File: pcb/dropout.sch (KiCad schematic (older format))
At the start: 61 parts, among them SW1 Rotary_Encoder_Switch, SW2 SW_Push, U1 ProMicro

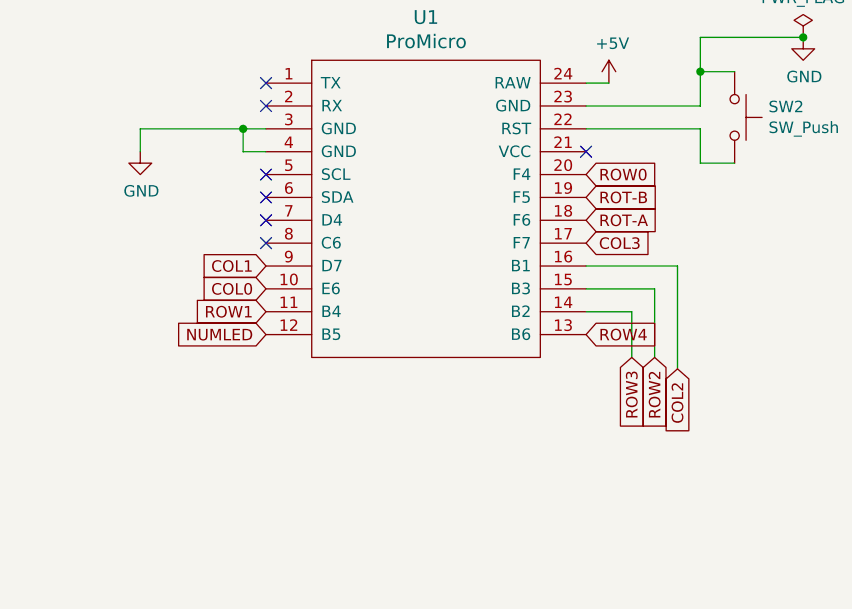
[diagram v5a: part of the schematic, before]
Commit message: flipping orientation of promicro for better clearance, now uses same pinout as rev0.1
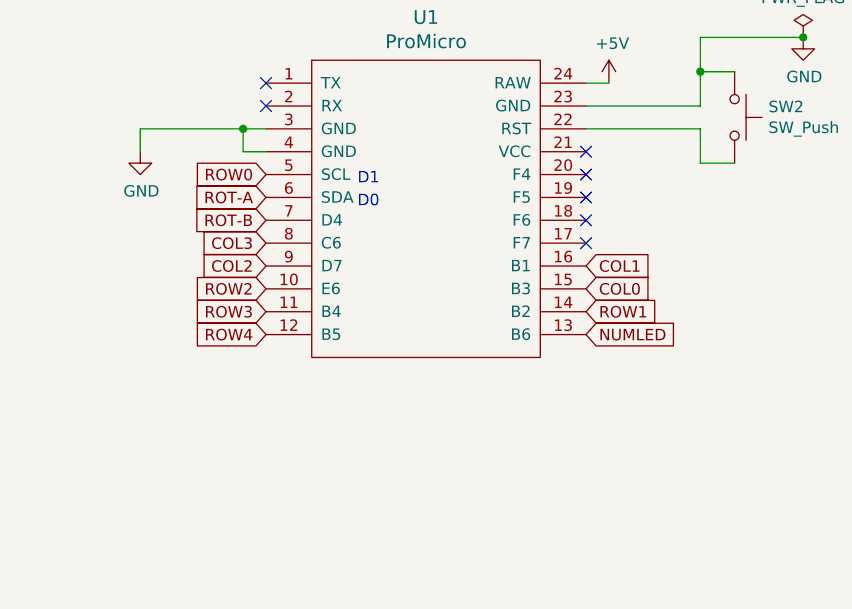
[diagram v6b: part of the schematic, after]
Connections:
- net COL0: now also U1.15 (B3); no longer U1.10 (E6)
- net COL1: now also U1.16 (B1); no longer U1.9 (D7)
- net COL2: now also U1.9 (D7); no longer U1.16 (B1)
- net COL3: now also U1.8 (C6); no longer U1.17 (F7)
- net NUMLED: now also U1.13 (B6); no longer U1.12 (B5)
- net ROT-A: now also U1.6 (SDA); no longer U1.18 (F6)
- net ROT-B: now also U1.7 (D4); no longer U1.19 (F5)
- net ROW0: now also U1.5 (SCL); no longer U1.20 (F4)
- net ROW1: now also U1.14 (B2); no longer U1.11 (B4)
- net ROW2: now also U1.10 (E6); no longer U1.15 (B3)
- net ROW3: now also U1.11 (B4); no longer U1.14 (B2)
- net ROW4: now also U1.12 (B5); no longer U1.13 (B6)
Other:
- note added: "D0"
- note added: "D1"
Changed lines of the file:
@@
 Wire Wire Line
 	4800 3350 4800 4200
-Text GLabel 5750 1850 2    50   Input ~ 0
-ROT-A
-Text GLabel 5750 1650 2    50   Input ~ 0
-ROT-B
 $Comp
 L power:GND #PWR03
@@
 	1    0    0    -1
 $EndComp
-$Comp
-L promicro:ProMicro U1
-U 1 1 5FCF7876
-P 7850 3750
-F 0 "U1" H 7850 4787 60  0000 C CNN
-F 1 "ProMicro" H 7850 4681 60  0000 C CNN
-F 2 "promicro:ProMico_mini&micro" H 7950 2700 60  0001 C CNN
-F 3 "" H 7950 2700 60  0000 C CNN
-	1    7850 3750
-	1    0    0    -1
-$EndComp
 Wire Wire Line
 	8550 3100 9050 3100
@@
 Wire Wire Line
 	6150 1750 6150 1950
-Text GLabel 8550 4100 2    50   Input ~ 0
+Text GLabel 7150 4100 0    50   Input ~ 0
 ROW4
-Text GLabel 8750 4200 3    50   Input ~ 0
+Text GLabel 7150 4000 0    50   Input ~ 0
 ROW3
-Text GLabel 8850 4200 3    50   Input ~ 0
+Text GLabel 7150 3900 0    50   Input ~ 0
 ROW2
-Text GLabel 7150 4000 0    50   Input ~ 0
+Text GLabel 8550 4000 2    50   Input ~ 0
 ROW1
-Text GLabel 8550 3400 2    50   Input ~ 0
+Text GLabel 7150 3400 0    50   Input ~ 0
 ROW0
-Text GLabel 7150 3900 0    50   Input ~ 0
+Text GLabel 8550 3900 2    50   Input ~ 0
 COL0
+Text GLabel 8550 3800 2    50   Input ~ 0
+COL1
 Text GLabel 7150 3800 0    50   Input ~ 0
-COL1
-Text GLabel 8950 4250 3    50   Input ~ 0
 COL2
 Text GLabel 4800 1050 1    50   Input ~ 0
 COL3
-Text GLabel 8550 3700 2    50   Input ~ 0
+Text GLabel 7150 3700 0    50   Input ~ 0
 COL3
-Text GLabel 7150 4100 0    50   Input ~ 0
+Text GLabel 8550 4100 2    50   Input ~ 0
 NUMLED
 $Comp
@@
 	1    0    0    -1
 $EndComp
-NoConn ~ 7150 3600
-NoConn ~ 7150 3700
 Wire Wire Line
 	4800 1050 4800 1400
-Wire Wire Line
-	8750 4200 8750 4000
-Wire Wire Line
-	8750 4000 8550 4000
-Wire Wire Line
-	8850 4200 8850 3900
-Wire Wire Line
-	8850 3900 8550 3900
-Wire Wire Line
-	8550 3800 8950 3800
-Wire Wire Line
-	8950 4250 8950 3800
 $Comp
 L Device:C C2
@@
 $EndComp
 Connection ~ 4800 1400
-Text GLabel 8550 3500 2    50   Input ~ 0
+Text GLabel 7150 3600 0    50   Input ~ 0
 ROT-B
-Text GLabel 8550 3600 2    50   Input ~ 0
+Text GLabel 7150 3500 0    50   Input ~ 0
 ROT-A
 Wire Wire Line
@@
 $EndComp
 Connection ~ 9500 2800
-NoConn ~ 7150 3400
-NoConn ~ 7150 3500
 NoConn ~ 8550 3300
+$Comp
+L promicro:ProMicro U1
+U 1 1 5FCF7876
+P 7850 3750
+F 0 "U1" H 7850 4787 60  0000 C CNN
+F 1 "ProMicro" H 7850 4681 60  0000 C CNN
+F 2 "promicro:ProMico_mini&micro" H 7950 2700 60  0001 C CNN
+F 3 "" H 7950 2700 60  0000 C CNN
+	1    7850 3750
+	1    0    0    -1
+$EndComp
+Text Notes 7550 3450 0    50   ~ 0
+D1
+Text Notes 7550 3550 0    50   ~ 0
+D0
+NoConn ~ 8550 3700
+NoConn ~ 8550 3600
+NoConn ~ 8550 3500
+NoConn ~ 8550 3400
+Text GLabel 5750 1850 2    50   Input ~ 0
+ROT-A
+Text GLabel 5750 1650 2    50   Input ~ 0
+ROT-B
 $EndSCHEMATC

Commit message: adding graphics to pcb, some cleanup
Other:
- note removed: "mini-usb\n"
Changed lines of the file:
@@
 Text Notes 9950 1200 0    50   ~ 0
 Holes for Base
-Text Notes 7700 2650 0    50   ~ 0
-mini-usb\n
 $Comp
 L MX_Alps_Hybrid:MX-NoLED K-FN1

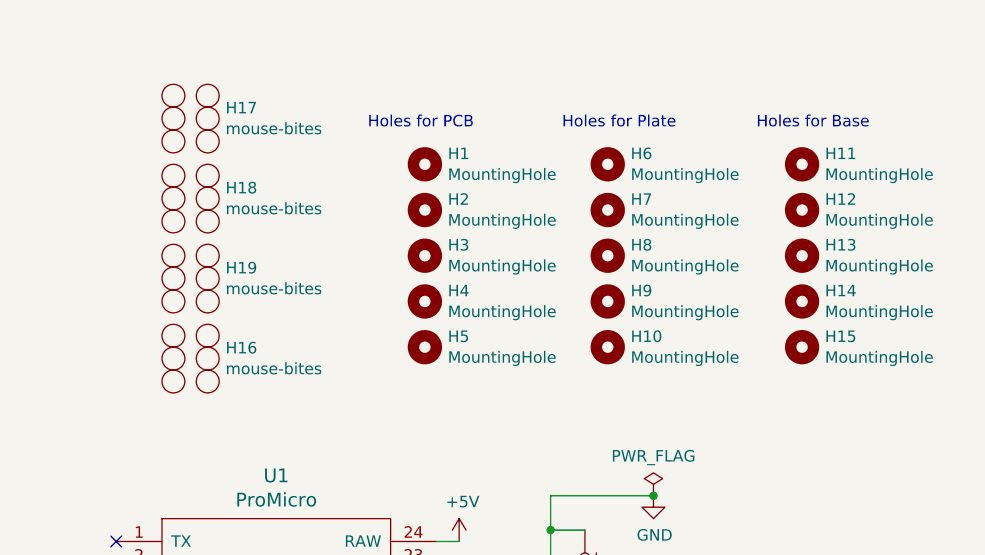
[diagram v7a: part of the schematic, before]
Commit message: breaking up panelization for production
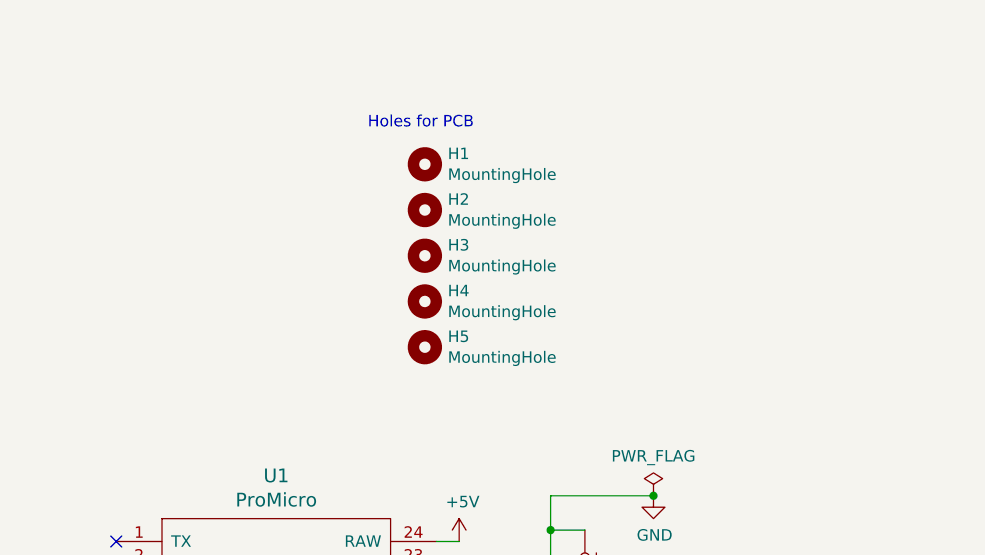
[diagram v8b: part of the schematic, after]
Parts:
- removed H10, H11, H12, H13, H14, H15, H6, H7, H8, H9: MountingHole, MountingHole:MountingHole_2.2mm_M2, symbol Mechanical:MountingHole
- removed H16, H17, H18, H19: mouse-bites, Keebio-Parts:breakaway-mousebites, symbol panelization:mouse-bites
- D1, D10, D11, D12, D13, D14, D15, D16, D17, D18, D2, D3, D4, D5, D6, D7, D8, D9: footprint footprint:Diode_TH_SOD123 -> Diodes_SMD:Diode_TH_SOD123
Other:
- note removed: "Holes for Base"
- note removed: "Holes for Plate"
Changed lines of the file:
@@
 F 0 "D6" H 2900 2067 50  0000 C CNN
 F 1 "D" H 2900 1976 50  0000 C CNN
-F 2 "footprint:Diode_TH_SOD123" H 2900 1850 50  0001 C CNN
+F 2 "Diodes_SMD:Diode_TH_SOD123" H 2900 1850 50  0001 C CNN
 F 3 "~" H 2900 1850 50  0001 C CNN
 	1    2900 1850
@@
 F 0 "D1" H 1950 2067 50  0000 C CNN
 F 1 "D" H 1950 1976 50  0000 C CNN
-F 2 "footprint:Diode_TH_SOD123" H 1950 1850 50  0001 C CNN
+F 2 "Diodes_SMD:Diode_TH_SOD123" H 1950 1850 50  0001 C CNN
 F 3 "~" H 1950 1850 50  0001 C CNN
 	1    1950 1850
@@
 F 0 "D10" H 3700 2067 50  0000 C CNN
 F 1 "D" H 3700 1976 50  0000 C CNN
-F 2 "footprint:Diode_TH_SOD123" H 3700 1850 50  0001 C CNN
+F 2 "Diodes_SMD:Diode_TH_SOD123" H 3700 1850 50  0001 C CNN
 F 3 "~" H 3700 1850 50  0001 C CNN
 	1    3700 1850
@@
 F 0 "D15" H 4450 2067 50  0000 C CNN
 F 1 "D" H 4450 1976 50  0000 C CNN
-F 2 "footprint:Diode_TH_SOD123" H 4450 1850 50  0001 C CNN
+F 2 "Diodes_SMD:Diode_TH_SOD123" H 4450 1850 50  0001 C CNN
 F 3 "~" H 4450 1850 50  0001 C CNN
 	1    4450 1850
@@
 F 0 "D2" H 1950 3067 50  0000 C CNN
 F 1 "D" H 1950 2976 50  0000 C CNN
-F 2 "footprint:Diode_TH_SOD123" H 1950 2850 50  0001 C CNN
+F 2 "Diodes_SMD:Diode_TH_SOD123" H 1950 2850 50  0001 C CNN
 F 3 "~" H 1950 2850 50  0001 C CNN
 	1    1950 2850
@@
 F 0 "D7" H 2900 3067 50  0000 C CNN
 F 1 "D" H 2900 2976 50  0000 C CNN
-F 2 "footprint:Diode_TH_SOD123" H 2900 2850 50  0001 C CNN
+F 2 "Diodes_SMD:Diode_TH_SOD123" H 2900 2850 50  0001 C CNN
 F 3 "~" H 2900 2850 50  0001 C CNN
 	1    2900 2850
@@
 F 0 "D11" H 3700 3067 50  0000 C CNN
 F 1 "D" H 3700 2976 50  0000 C CNN
-F 2 "footprint:Diode_TH_SOD123" H 3700 2850 50  0001 C CNN
+F 2 "Diodes_SMD:Diode_TH_SOD123" H 3700 2850 50  0001 C CNN
 F 3 "~" H 3700 2850 50  0001 C CNN
 	1    3700 2850
@@
 F 0 "D16" H 4450 3067 50  0000 C CNN
 F 1 "D" H 4450 2976 50  0000 C CNN
-F 2 "footprint:Diode_TH_SOD123" H 4450 2850 50  0001 C CNN
+F 2 "Diodes_SMD:Diode_TH_SOD123" H 4450 2850 50  0001 C CNN
 F 3 "~" H 4450 2850 50  0001 C CNN
 	1    4450 2850
@@
 F 0 "D3" H 1950 3967 50  0000 C CNN
 F 1 "D" H 1950 3876 50  0000 C CNN
-F 2 "footprint:Diode_TH_SOD123" H 1950 3750 50  0001 C CNN
+F 2 "Diodes_SMD:Diode_TH_SOD123" H 1950 3750 50  0001 C CNN
 F 3 "~" H 1950 3750 50  0001 C CNN
 	1    1950 3750
@@
 F 0 "D8" H 2900 3967 50  0000 C CNN
 F 1 "D" H 2900 3876 50  0000 C CNN
-F 2 "footprint:Diode_TH_SOD123" H 2900 3750 50  0001 C CNN
+F 2 "Diodes_SMD:Diode_TH_SOD123" H 2900 3750 50  0001 C CNN
 F 3 "~" H 2900 3750 50  0001 C CNN
 	1    2900 3750
@@
 F 0 "D12" H 3700 3967 50  0000 C CNN
 F 1 "D" H 3700 3876 50  0000 C CNN
-F 2 "footprint:Diode_TH_SOD123" H 3700 3750 50  0001 C CNN
+F 2 "Diodes_SMD:Diode_TH_SOD123" H 3700 3750 50  0001 C CNN
 F 3 "~" H 3700 3750 50  0001 C CNN
 	1    3700 3750
@@
 F 0 "D17" H 4450 3967 50  0000 C CNN
 F 1 "D" H 4450 3876 50  0000 C CNN
-F 2 "footprint:Diode_TH_SOD123" H 4450 3750 50  0001 C CNN
+F 2 "Diodes_SMD:Diode_TH_SOD123" H 4450 3750 50  0001 C CNN
 F 3 "~" H 4450 3750 50  0001 C CNN
 	1    4450 3750
@@
 F 0 "D4" H 1950 4817 50  0000 C CNN
 F 1 "D" H 1950 4726 50  0000 C CNN
-F 2 "footprint:Diode_TH_SOD123" H 1950 4600 50  0001 C CNN
+F 2 "Diodes_SMD:Diode_TH_SOD123" H 1950 4600 50  0001 C CNN
 F 3 "~" H 1950 4600 50  0001 C CNN
 	1    1950 4600
@@
 F 0 "D9" H 2900 4817 50  0000 C CNN
 F 1 "D" H 2900 4726 50  0000 C CNN
-F 2 "footprint:Diode_TH_SOD123" H 2900 4600 50  0001 C CNN
+F 2 "Diodes_SMD:Diode_TH_SOD123" H 2900 4600 50  0001 C CNN
 F 3 "~" H 2900 4600 50  0001 C CNN
 	1    2900 4600
@@
 F 0 "D13" H 3700 4817 50  0000 C CNN
 F 1 "D" H 3700 4726 50  0000 C CNN
-F 2 "footprint:Diode_TH_SOD123" H 3700 4600 50  0001 C CNN
+F 2 "Diodes_SMD:Diode_TH_SOD123" H 3700 4600 50  0001 C CNN
 F 3 "~" H 3700 4600 50  0001 C CNN
 	1    3700 4600
@@
 F 0 "D18" H 4450 4817 50  0000 C CNN
 F 1 "D" H 4450 4726 50  0000 C CNN
-F 2 "footprint:Diode_TH_SOD123" H 4450 4600 50  0001 C CNN
+F 2 "Diodes_SMD:Diode_TH_SOD123" H 4450 4600 50  0001 C CNN
 F 3 "~" H 4450 4600 50  0001 C CNN
 	1    4450 4600
@@
 F 0 "D5" H 1950 5667 50  0000 C CNN
 F 1 "D" H 1950 5576 50  0000 C CNN
-F 2 "footprint:Diode_TH_SOD123" H 1950 5450 50  0001 C CNN
+F 2 "Diodes_SMD:Diode_TH_SOD123" H 1950 5450 50  0001 C CNN
 F 3 "~" H 1950 5450 50  0001 C CNN
 	1    1950 5450
@@
 F 0 "D14" H 3700 5667 50  0000 C CNN
 F 1 "D" H 3700 5576 50  0000 C CNN
-F 2 "footprint:Diode_TH_SOD123" H 3700 5450 50  0001 C CNN
+F 2 "Diodes_SMD:Diode_TH_SOD123" H 3700 5450 50  0001 C CNN
 F 3 "~" H 3700 5450 50  0001 C CNN
 	1    3700 5450
@@
 Wire Wire Line
 	5700 1350 6250 1350
-$Comp
-L Mechanical:MountingHole H6
-U 1 1 5FCEF804
-P 9300 1350
-F 0 "H6" H 9400 1396 50  0000 L CNN
-F 1 "MountingHole" H 9400 1305 50  0000 L CNN
-F 2 "MountingHole:MountingHole_2.2mm_M2" H 9300 1350 50  0001 C CNN
-F 3 "~" H 9300 1350 50  0001 C CNN
-	1    9300 1350
-	1    0    0    -1
-$EndComp
-$Comp
-L Mechanical:MountingHole H7
-U 1 1 5FCEFF4E
-P 9300 1550
-F 0 "H7" H 9400 1596 50  0000 L CNN
-F 1 "MountingHole" H 9400 1505 50  0000 L CNN
-F 2 "MountingHole:MountingHole_2.2mm_M2" H 9300 1550 50  0001 C CNN
-F 3 "~" H 9300 1550 50  0001 C CNN
-	1    9300 1550
-	1    0    0    -1
-$EndComp
-$Comp
-L Mechanical:MountingHole H8
-U 1 1 5FCF347A
-P 9300 1750
-F 0 "H8" H 9400 1796 50  0000 L CNN
-F 1 "MountingHole" H 9400 1705 50  0000 L CNN
-F 2 "MountingHole:MountingHole_2.2mm_M2" H 9300 1750 50  0001 C CNN
-F 3 "~" H 9300 1750 50  0001 C CNN
-	1    9300 1750
-	1    0    0    -1
-$EndComp
-$Comp
-L Mechanical:MountingHole H9
-U 1 1 5FCF6A76
-P 9300 1950
-F 0 "H9" H 9400 1996 50  0000 L CNN
-F 1 "MountingHole" H 9400 1905 50  0000 L CNN
-F 2 "MountingHole:MountingHole_2.2mm_M2" H 9300 1950 50  0001 C CNN
-F 3 "~" H 9300 1950 50  0001 C CNN
-	1    9300 1950
-	1    0    0    -1
-$EndComp
-$Comp
-L Mechanical:MountingHole H10
-U 1 1 5FCF9F59
-P 9300 2150
-F 0 "H10" H 9400 2196 50  0000 L CNN
-F 1 "MountingHole" H 9400 2105 50  0000 L CNN
-F 2 "MountingHole:MountingHole_2.2mm_M2" H 9300 2150 50  0001 C CNN
-F 3 "~" H 9300 2150 50  0001 C CNN
-	1    9300 2150
-	1    0    0    -1
-$EndComp
-$Comp
-L Mechanical:MountingHole H11
-U 1 1 5FCFE769
-P 10150 1350
-F 0 "H11" H 10250 1396 50  0000 L CNN
-F 1 "MountingHole" H 10250 1305 50  0000 L CNN
-F 2 "MountingHole:MountingHole_2.2mm_M2" H 10150 1350 50  0001 C CNN
-F 3 "~" H 10150 1350 50  0001 C CNN
-	1    10150 1350
-	1    0    0    -1
-$EndComp
-$Comp
-L Mechanical:MountingHole H12
-U 1 1 5FCFE76F
-P 10150 1550
-F 0 "H12" H 10250 1596 50  0000 L CNN
-F 1 "MountingHole" H 10250 1505 50  0000 L CNN
-F 2 "MountingHole:MountingHole_2.2mm_M2" H 10150 1550 50  0001 C CNN
-F 3 "~" H 10150 1550 50  0001 C CNN
-	1    10150 1550
-	1    0    0    -1
-$EndComp
-$Comp
-L Mechanical:MountingHole H13
-U 1 1 5FCFE775
-P 10150 1750
-F 0 "H13" H 10250 1796 50  0000 L CNN
-F 1 "MountingHole" H 10250 1705 50  0000 L CNN
-F 2 "MountingHole:MountingHole_2.2mm_M2" H 10150 1750 50  0001 C CNN
-F 3 "~" H 10150 1750 50  0001 C CNN
-	1    10150 1750
-	1    0    0    -1
-$EndComp
-$Comp
-L Mechanical:MountingHole H14
-U 1 1 5FCFE77B
-P 10150 1950
-F 0 "H14" H 10250 1996 50  0000 L CNN
-F 1 "MountingHole" H 10250 1905 50  0000 L CNN
-F 2 "MountingHole:MountingHole_2.2mm_M2" H 10150 1950 50  0001 C CNN
-F 3 "~" H 10150 1950 50  0001 C CNN
-	1    10150 1950
-	1    0    0    -1
-$EndComp
-$Comp
-L Mechanical:MountingHole H15
-U 1 1 5FCFE781
-P 10150 2150
-F 0 "H15" H 10250 2196 50  0000 L CNN
-F 1 "MountingHole" H 10250 2105 50  0000 L CNN
-F 2 "MountingHole:MountingHole_2.2mm_M2" H 10150 2150 50  0001 C CNN
-F 3 "~" H 10150 2150 50  0001 C CNN
-	1    10150 2150
-	1    0    0    -1
-$EndComp
 Text Notes 8250 1200 0    50   ~ 0
 Holes for PCB
-Text Notes 9100 1200 0    50   ~ 0
-Holes for Plate
-Text Notes 9950 1200 0    50   ~ 0
-Holes for Base
 $Comp
 L MX_Alps_Hybrid:MX-NoLED K-FN1
@@
 	9050 2950 9050 2800
 $Comp
-L panelization:mouse-bites H19
-U 1 1 5FE6A655
-P 7500 1600
-F 0 "H19" H 7628 1396 50  0000 L CNN
-F 1 "mouse-bites" H 7628 1305 50  0000 L CNN
-F 2 "Keebio-Parts:breakaway-mousebites" H 7500 1600 50  0001 C CNN
-F 3 "" H 7500 1600 50  0001 C CNN
-	1    7500 1600
-	1    0    0    -1
-$EndComp
-$Comp
-L panelization:mouse-bites H18
-U 1 1 5FE6A2C7
-P 7500 1250
-F 0 "H18" H 7628 1046 50  0000 L CNN
-F 1 "mouse-bites" H 7628 955 50  0000 L CNN
-F 2 "Keebio-Parts:breakaway-mousebites" H 7500 1250 50  0001 C CNN
-F 3 "" H 7500 1250 50  0001 C CNN
-	1    7500 1250
-	1    0    0    -1
-$EndComp
-$Comp
-L panelization:mouse-bites H17
-U 1 1 5FE69F24
-P 7500 900
-F 0 "H17" H 7628 696 50  0000 L CNN
-F 1 "mouse-bites" H 7628 605 50  0000 L CNN
-F 2 "Keebio-Parts:breakaway-mousebites" H 7500 900 50  0001 C CNN
-F 3 "" H 7500 900 50  0001 C CNN
-	1    7500 900
-	1    0    0    -1
-$EndComp
-$Comp
-L panelization:mouse-bites H16
-U 1 1 5FE6952B
-P 7500 1950
-F 0 "H16" H 7628 1746 50  0000 L CNN
-F 1 "mouse-bites" H 7628 1655 50  0000 L CNN
-F 2 "Keebio-Parts:breakaway-mousebites" H 7500 1950 50  0001 C CNN
-F 3 "" H 7500 1950 50  0001 C CNN
-	1    7500 1950
-	1    0    0    -1
-$EndComp
-$Comp
 L power:GND #PWR08
